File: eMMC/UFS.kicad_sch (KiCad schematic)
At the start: 1 part, among them J1 Barrel_Jack_Switch

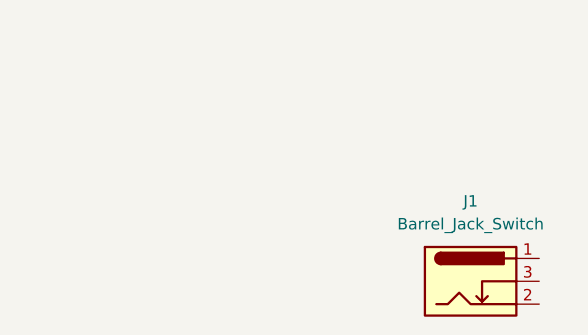
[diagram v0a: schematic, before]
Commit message: Replace v2 with correct source: RK3576_SBCv2 (Copy) (2)
- Delete previous v2 files, upload cleaned (2) version
- Restore eMMC/ and UFS/ storage sheets
- Drop connectors, dc_power_soket, digital, fixtures, power placeholders
- Update RK3576 SBCv2.kicad_pro
- Exclude: .history (141M), Resources ref PDF, *.bak, *.lck
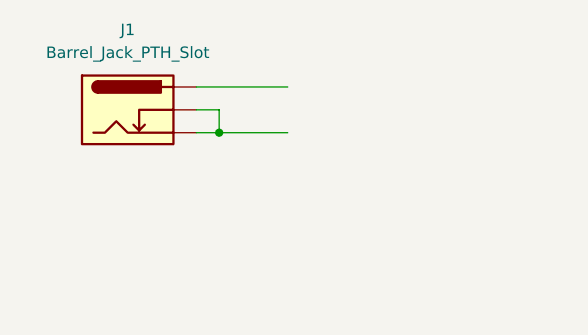
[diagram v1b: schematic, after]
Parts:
- removed J1: Barrel_Jack_Switch, Connector_BarrelJack:BarrelJack_CUI_PJ-063AH_Horizontal, symbol Connector:Barrel_Jack_Switch
- added J1: Barrel_Jack_PTH_Slot, PCM_SparkFun-Connector:Barrel_Jack_PTH_Slot, symbol PCM_SparkFun-Connector:Barrel_Jack_PTH_Slot
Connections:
- new net: J1.GND, J1.GNDBREAK
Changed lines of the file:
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@@
 	(generator_version "10.0")
 	(paper "A4")
+	(junction
+		(at 46.99 59.69)
+		(diameter 0)
+		(color 0 0 0 0)
+	)
+	(wire
+		(pts
+			(xy 46.99 59.69) (xy 54.61 59.69)
+		)
+		(stroke
+			(width 0)
+			(type default)
+		)
+	)
+	(wire
+		(pts
+			(xy 46.99 57.15) (xy 46.99 59.69)
+		)
+		(stroke
+			(width 0)
+			(type default)
+		)
+	)
+	(wire
+		(pts
+			(xy 44.45 54.61) (xy 54.61 54.61)
+		)
+		(stroke
+			(width 0)
+			(type default)
+		)
+	)
+	(wire
+		(pts
+			(xy 44.45 59.69) (xy 46.99 59.69)
+		)
+		(stroke
+			(width 0)
+			(type default)
+		)
+	)
+	(wire
+		(pts
+			(xy 44.45 57.15) (xy 46.99 57.15)
+		)
+		(stroke
+			(width 0)
+			(type default)
+		)
+	)
 	(symbol
-		(lib_id "Connector:Barrel_Jack_Switch")
-		(at 74.93 76.2 0)
+		(lib_id "PCM_SparkFun-Connector:Barrel_Jack_PTH_Slot")
+		(at 36.83 57.15 0)
 		(unit 1)
 		(body_style 1)
@@
 		(fields_autoplaced yes)
 		(property "Reference" "J1"
-			(at 74.93 67.31 0)
+			(at 36.83 48.26 0)
 			(show_name no)
 			(do_not_autoplace no)
@@
 			)
 		)
-		(property "Value" "Barrel_Jack_Switch"
-			(at 74.93 69.85 0)
+		(property "Value" "Barrel_Jack_PTH_Slot"
+			(at 36.83 50.8 0)
 			(show_name no)
 			(do_not_autoplace no)
@@
 			)
 		)
-		(property "Footprint" "Connector_BarrelJack:BarrelJack_CUI_PJ-063AH_Horizontal"
-			(at 76.2 77.216 0)
+		(property "Footprint" "PCM_SparkFun-Connector:Barrel_Jack_PTH_Slot"
+			(at 36.83 67.31 0)
 			(hide yes)
 			(show_name no)
@@
 			)
 		)
-		(property "Datasheet" ""
-			(at 76.2 77.216 0)
+		(property "Datasheet" "https://www.sparkfun.com/datasheets/Prototyping/Barrel-Connector-PJ-202A.pdf"
+			(at 36.83 69.85 0)
 			(hide yes)
 			(show_name no)
@@
 		)
 		(property "Description" "DC Barrel Jack with an internal switch"
-			(at 74.93 76.2 0)
+			(at 36.83 72.39 0)
 			(hide yes)
 			(show_name no)
@@
 			)
 		)
-		(pin "1"
+		(property "PROD_ID" "CONN-08197"
+			(at 36.83 64.77 0)
+			(hide yes)
+			(show_name no)
+			(do_not_autoplace no)
+			(effects
+				(font
+					(size 1.27 1.27)
+				)
+			)
 		)
-		(pin "3"
+		(pin "PWR"
 		)
-		(pin "2"
+		(pin "GNDBREAK"
+		)
+		(pin "GND"
 		)
 		(instances
 			(project "RK3576 SBCv2"
+				(path "/802f5b9f-44c6-4b1a-a63a-2c094d5816db/18e487aa-7d5d-4330-b69d-f75c2ebdb2cf"
+					(reference "J3")
+					(unit 1)
+				)
 				(path "/802f5b9f-44c6-4b1a-a63a-2c094d5816db/976da9c6-11e1-4e8a-b7c7-c3dc062804e4"
 					(reference "J1")
